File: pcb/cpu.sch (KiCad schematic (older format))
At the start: 76 parts, among them J1 Conn_02x16_Counter_Clockwise, J2 Conn_01x16, U1 74LS283, U2 74LS283, U3 74LS283, U4 74LS283

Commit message: alu function
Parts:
- removed U? (x4): mux16, symbol nand2tetris:mux16
- removed U? (x16): 74AHCT1G04, symbol 74xGxx:74AHCT1G04
- added U? (x3): SN74CBT16233, symbol nand2tetris:SN74CBT16233
- added U? (x32): 74AHCT1G04, symbol 74xGxx:74AHCT1G04
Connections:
- net a0 is gone; now on net x0: J1.1 (Pin_1)
- net a1 is gone; now on net x1: J1.2 (Pin_2)
- net a10 is gone; now on net x10: J1.11 (Pin_11)
- net a11 is gone; now on net x11: J1.12 (Pin_12)
- net a12 is gone; now on net x12: J1.13 (Pin_13)
- net a13 is gone; now on net x13: J1.14 (Pin_14)
- net a14 is gone; now on net x14: J1.15 (Pin_15)
- net a15 is gone; now on net x15: J1.16 (Pin_16)
- net a2 is gone; now on net x2: J1.3 (Pin_3)
- net a3 is gone; now on net x3: J1.4 (Pin_4)
- net a4 is gone; now on net x4: J1.5 (Pin_5)
- net a5 is gone; now on net x5: J1.6 (Pin_6)
- net a6 is gone; now on net x6: J1.7 (Pin_7)
- net a7 is gone; now on net x7: J1.8 (Pin_8)
- net a8 is gone; now on net x8: J1.9 (Pin_9)
- net a9 is gone; now on net x9: J1.10 (Pin_10)
- net b0 is gone; now on net y0: J1.32 (Pin_32)
- net b1 is gone; now on net y1: J1.31 (Pin_31)
- net b10 is gone; now on net y10: J1.22 (Pin_22)
- net b11 is gone; now on net y11: J1.21 (Pin_21)
- net b12 is gone; now on net y12: J1.20 (Pin_20)
- net b13 is gone; now on net y13: J1.19 (Pin_19)
- net b14 is gone; now on net y14: J1.18 (Pin_18)
- net b15 is gone; now on net y15: J1.17 (Pin_17)
- net b2 is gone; now on net y2: J1.30 (Pin_30)
- net b3 is gone; now on net y3: J1.29 (Pin_29)
- net b4 is gone; now on net y4: J1.28 (Pin_28)
- net b5 is gone; now on net y5: J1.27 (Pin_27)
- net b6 is gone; now on net y6: J1.26 (Pin_26)
- net b7 is gone; now on net y7: J1.25 (Pin_25)
- net b8 is gone; now on net y8: J1.24 (Pin_24)
- net b9 is gone; now on net y9: J1.23 (Pin_23)
- net noty0 is gone; now on an unnamed net: U?.4
- net noty1 is gone; now on an unnamed net: U?.4
- net noty10 is gone; now on an unnamed net: U?.4
- net noty11 is gone; now on an unnamed net: U?.4
- net noty12 is gone; now on an unnamed net: U?.4
- net noty13 is gone; now on an unnamed net: U?.4
- net noty14 is gone; now on an unnamed net: U?.4
- net noty15 is gone; now on an unnamed net: U?.4
- net noty2 is gone; now on an unnamed net: U?.4
- net noty3 is gone; now on an unnamed net: U?.4
- net noty4 is gone; now on an unnamed net: U?.4
- net noty5 is gone; now on an unnamed net: U?.4
- net noty6 is gone; now on an unnamed net: U?.4
- net noty7 is gone; now on an unnamed net: U?.4
- net noty8 is gone; now on an unnamed net: U?.4
- net noty9 is gone; now on an unnamed net: U?.4
- net GND: now also U?.44 (GND), U?.3 (GND), U?.3 (GND), U?.3 (GND), U?.3 (GND), U?.3 (GND), U?.3 (GND), U?.3 (GND), U?.3 (GND), U?.3 (GND), U?.3 (GND), U?.3 (GND), U?.3 (GND), U?.3 (GND), U?.3 (GND), U?.3 (GND), U?.3 (GND), U?.3 (GND), U?.3 (GND), U?.3 (GND), U?.3 (GND), U?.3 (GND), U?.3 (GND), U?.3 (GND), U?.3 (GND), U?.3 (GND), U?.3 (GND), U?.3 (GND), U?.3 (GND), U?.3 (GND), U?.3 (GND), U?.3 (GND), U?.3 (GND), U?.44 (GND), U?.44 (GND), U?.44 (GND)
- net VCC: now also U?.43 (VCC), U?.43 (VCC), U?.43 (VCC), U?.43 (VCC), U?.5 (VCC), U?.5 (VCC), U?.5 (VCC), U?.5 (VCC), U?.5 (VCC), U?.5 (VCC), U?.5 (VCC), U?.5 (VCC), U?.5 (VCC), U?.5 (VCC), U?.5 (VCC), U?.5 (VCC), U?.5 (VCC), U?.5 (VCC), U?.5 (VCC), U?.5 (VCC), U?.5 (VCC), U?.5 (VCC), U?.5 (VCC), U?.5 (VCC), U?.5 (VCC), U?.5 (VCC), U?.5 (VCC), U?.5 (VCC), U?.5 (VCC), U?.5 (VCC), U?.5 (VCC), U?.5 (VCC), U?.5 (VCC), U?.5 (VCC), U?.5 (VCC), U?.5 (VCC)
- net band0: now also U?.2
- net band1: now also U?.2
- net band10: now also U?.2
- net band11: now also U?.2
- net band12: now also U?.2
- net band13: now also U?.2
- net band14: now also U?.2
- net band15: now also U?.2
- net band2: now also U?.2
- net band3: now also U?.2
- net band4: now also U?.2
- net band5: now also U?.2
- net band6: now also U?.2
- net band7: now also U?.2
- net band8: no longer U?.3
- net band9: now also U?.2
- net nx: now also U?.30 (SEL1)
- net ny: now also U?.30 (SEL1)
- net opx0: now also U?.1 (1A)
- net opx1: now also U?.54 (2A)
- net opx10: now also U?.18 (11A)
- net opx11: now also U?.37 (12A)
- net opx12: now also U?.21 (13A)
- net opx13: now also U?.34 (14A)
- net opx14: now also U?.24 (15A)
- net opx15: now also U?.31 (16A)
- net opx2: now also U?.4 (3A)
- net opx3: now also U?.51 (4A)
- net opx4: now also U?.7 (5A)
- net opx5: now also U?.48 (6A)
- net opx6: now also U?.10 (7A)
- net opx7: now also U?.45 (8A)
- net opx8: now also U?.15 (9A)
- net opx9: now also U?.40 (10A)
- net zdx0: now also U?.1 (1A), U?.2, U?.56 (1B1)
- net zdx1: now also U?.2, U?.2 (2B1), U?.54 (2A)
- net zdx10: now also U?.18 (11A), U?.2, U?.39 (11B1)
- net zdx11: now also U?.19 (12B1), U?.2, U?.37 (12A)
- net zdx12: now also U?.2, U?.21 (13A), U?.36 (13B1)
- net zdx13: now also U?.2, U?.22 (14B1), U?.34 (14A)
- net zdx14: now also U?.2, U?.24 (15A), U?.33 (15B1)
- net zdx15: now also U?.2, U?.25 (16B1), U?.31 (16A)
- net zdx2: now also U?.2, U?.4 (3A), U?.53 (3B1)
- net zdx3: now also U?.2, U?.5 (4B1), U?.51 (4A)
- net zdx4: now also U?.2, U?.50 (5B1), U?.7 (5A)
- net zdx5: now also U?.2, U?.48 (6A), U?.8 (6B1)
- net zdx6: now also U?.10 (7A), U?.2, U?.47 (7B1)
- net zdx7: now also U?.11 (8B1), U?.2, U?.45 (8A)
- net zdx8: now also U?.15 (9A), U?.2, U?.42 (9B1)
- net zdx9: now also U?.16 (10B1), U?.2, U?.40 (10A)
- net zdy0: now also U?.56 (1B1), U?.1 (1A)
- net zdy1: now also U?.2 (2B1), U?.54 (2A)
- net zdy10: now also U?.39 (11B1), U?.18 (11A)
- net zdy11: now also U?.19 (12B1), U?.37 (12A)
- net zdy12: now also U?.36 (13B1), U?.21 (13A)
- net zdy13: now also U?.22 (14B1), U?.34 (14A)
- net zdy14: now also U?.33 (15B1), U?.24 (15A)
- net zdy15: now also U?.25 (16B1), U?.31 (16A)
- net zdy2: now also U?.53 (3B1), U?.4 (3A)
- net zdy3: now also U?.5 (4B1), U?.51 (4A)
- net zdy4: now also U?.50 (5B1), U?.7 (5A)
- net zdy5: now also U?.8 (6B1), U?.48 (6A)
- net zdy6: now also U?.47 (7B1), U?.10 (7A)
- net zdy7: now also U?.11 (8B1), U?.45 (8A)
- net zdy8: now also U?.42 (9B1), U?.15 (9A)
- net zdy9: now also U?.16 (10B1), U?.40 (10A)
- net zx: now also U?.30 (SEL1)
- net zy: now also U?.30 (SEL1)
- new net: U?.2, U?.3
- new net: U?.12 (8B2), U?.4
- new net: U?.4, U?.46 (7B2)
- new net: U?.4, U?.9 (6B2)
- new net: U?.4, U?.49 (5B2)
- new net: U?.4, U?.6 (4B2)
- new net: U?.4, U?.52 (3B2)
- new net: U?.3 (2B2), U?.4
- new net: U?.4, U?.55 (1B2)
- new net: U?.26 (16B2), U?.4
- new net: U?.32 (15B2), U?.4
- new net: U?.23 (14B2), U?.4
- new net: U?.35 (13B2), U?.4
- new net: U?.20 (12B2), U?.4
- new net: U?.38 (11B2), U?.4
- new net: U?.17 (10B2), U?.4
- new net: U?.4, U?.41 (9B2)
- new net notband0: U?.4
- new net notband1: U?.4
- new net notband10: U?.4
- new net notband11: U?.4
- new net notband12: U?.4
- new net notband13: U?.4
- new net notband14: U?.4
- new net notband15: U?.4
- new net notband2: U?.4
- new net notband3: U?.4
- new net notband4: U?.4
- new net notband5: U?.4
- new net notband6: U?.4
- new net notband7: U?.4
- new net notband8: U?.4
- new net notband9: U?.4
- no-connect marks 2 -> 22
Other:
- moved on the sheet: J1, J2, J?, U1, U2, U3, U4, U?, U?A

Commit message: output select
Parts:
- added U? (x3): SN74CBT16233, symbol nand2tetris:SN74CBT16233
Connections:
- net GND: now also U?.44 (GND), U?.44 (GND), U?.44 (GND)
- net VCC: now also U?.43 (VCC), U?.43 (VCC), U?.43 (VCC)
- net band0: now also U?.56 (1B1)
- net band1: now also U?.2 (2B1)
- net band10: now also U?.39 (11B1)
- net band11: now also U?.19 (12B1)
- net band12: now also U?.36 (13B1)
- net band13: now also U?.22 (14B1)
- net band14: now also U?.33 (15B1)
- net band15: now also U?.25 (16B1)
- net band2: now also U?.53 (3B1)
- net band3: now also U?.5 (4B1)
- net band4: now also U?.50 (5B1)
- net band5: now also U?.8 (6B1)
- net band6: now also U?.47 (7B1)
- net band7: now also U?.11 (8B1)
- net band8: now also U?.42 (9B1)
- net band9: now also U?.16 (10B1)
- net f: now also U?.30 (SEL1), U?.30 (SEL1)
- net no: now also U?.30 (SEL1)
- net notband0: now also U?.56 (1B1)
- net notband1: now also U?.2 (2B1)
- net notband10: now also U?.39 (11B1)
- net notband11: now also U?.19 (12B1)
- net notband12: now also U?.36 (13B1)
- net notband13: now also U?.22 (14B1)
- net notband14: now also U?.33 (15B1)
- net notband15: now also U?.25 (16B1)
- net notband2: now also U?.53 (3B1)
- net notband3: now also U?.5 (4B1)
- net notband4: now also U?.50 (5B1)
- net notband5: now also U?.8 (6B1)
- net notband6: now also U?.47 (7B1)
- net notband7: now also U?.11 (8B1)
- net notband8: now also U?.42 (9B1)
- net notband9: now also U?.16 (10B1)
- net sum0: now also U?.55 (1B2)
- net sum1: now also U?.3 (2B2)
- net sum10: now also U?.38 (11B2)
- net sum11: now also U?.20 (12B2)
- net sum12: now also U?.35 (13B2)
- net sum13: now also U?.23 (14B2)
- net sum14: now also U?.32 (15B2)
- net sum15: now also U?.26 (16B2)
- net sum2: now also U?.52 (3B2)
- net sum3: now also U?.6 (4B2)
- net sum4: now also U?.49 (5B2)
- net sum5: now also U?.9 (6B2)
- net sum6: now also U?.46 (7B2)
- net sum7: now also U?.12 (8B2)
- net sum8: now also U?.41 (9B2)
- net sum9: now also U?.17 (10B2)
- new net: U?.1 (1A), U?.56 (1B1)
- new net: U?.10 (7A), U?.47 (7B1)
- new net: U?.15 (9A), U?.42 (9B1)
- new net: U?.18 (11A), U?.39 (11B1)
- new net: U?.21 (13A), U?.36 (13B1)
- new net: U?.24 (15A), U?.33 (15B1)
- new net: U?.25 (16B1), U?.31 (16A)
- new net: U?.22 (14B1), U?.34 (14A)
- new net: U?.19 (12B1), U?.37 (12A)
- new net: U?.4 (3A), U?.53 (3B1)
- new net: U?.16 (10B1), U?.40 (10A)
- new net: U?.11 (8B1), U?.45 (8A)
- new net: U?.48 (6A), U?.8 (6B1)
- new net: U?.5 (4B1), U?.51 (4A)
- new net: U?.2 (2B1), U?.54 (2A)
- new net: U?.50 (5B1), U?.7 (5A)
- new net notsum: U?.12 (8B2), U?.17 (10B2), U?.20 (12B2), U?.23 (14B2), U?.26 (16B2), U?.3 (2B2), U?.32 (15B2), U?.35 (13B2), U?.38 (11B2), U?.41 (9B2), U?.46 (7B2), U?.49 (5B2), U?.52 (3B2), U?.55 (1B2), U?.6 (4B2), U?.9 (6B2)
- new net oalu0: U?.1 (1A)
- new net oalu1: U?.54 (2A)
- new net oalu10: U?.18 (11A)
- new net oalu11: U?.37 (12A)
- new net oalu12: U?.21 (13A)
- new net oalu13: U?.34 (14A)
- new net oalu14: U?.24 (15A)
- new net oalu15: U?.31 (16A)
- new net oalu2: U?.4 (3A)
- new net oalu3: U?.51 (4A)
- new net oalu4: U?.7 (5A)
- new net oalu5: U?.48 (6A)
- new net oalu6: U?.10 (7A)
- new net oalu7: U?.45 (8A)
- new net oalu8: U?.15 (9A)
- new net oalu9: U?.40 (10A)
- new net selnot0: U?.1 (1A), U?.55 (1B2)
- new net selnot1: U?.3 (2B2), U?.54 (2A)
- new net selnot10: U?.18 (11A), U?.38 (11B2)
- new net selnot11: U?.20 (12B2), U?.37 (12A)
- new net selnot12: U?.21 (13A), U?.35 (13B2)
- new net selnot13: U?.23 (14B2), U?.34 (14A)
- new net selnot14: U?.24 (15A), U?.32 (15B2)
- new net selnot15: U?.26 (16B2), U?.31 (16A)
- new net selnot2: U?.4 (3A), U?.52 (3B2)
- new net selnot3: U?.51 (4A), U?.6 (4B2)
- new net selnot4: U?.49 (5B2), U?.7 (5A)
- new net selnot5: U?.48 (6A), U?.9 (6B2)
- new net selnot6: U?.10 (7A), U?.46 (7B2)
- new net selnot7: U?.12 (8B2), U?.45 (8A)
- new net selnot8: U?.15 (9A), U?.41 (9B2)
- new net selnot9: U?.17 (10B2), U?.40 (10A)
- no-connect marks 22 -> 37

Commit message: ALU
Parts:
- added U? (x15): 74LS32, symbol 74xx:74LS32
- added U? (x15): 74LS02, symbol 74xx:74LS02
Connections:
- net oalu0: now also U?.2
- net oalu1: now also U?.3
- net oalu10: now also U?.2
- net oalu11: now also U?.3
- net oalu12: now also U?.2
- net oalu13: now also U?.3
- net oalu14: now also U?.2
- net oalu2: now also U?.2
- net oalu3: now also U?.3
- net oalu4: now also U?.2
- net oalu5: now also U?.3
- net oalu6: now also U?.2
- net oalu7: now also U?.3
- net oalu8: now also U?.2
- net oalu9: now also U?.3
- net oalu15 renamed ng
- net ng: now also U?.3
- new net: U?.1, U?.3 (x14)
- new net: U?.2, U?.3 (x7)
- new net: U?.1, U?.2 (x7)
- new net zr: U?.1

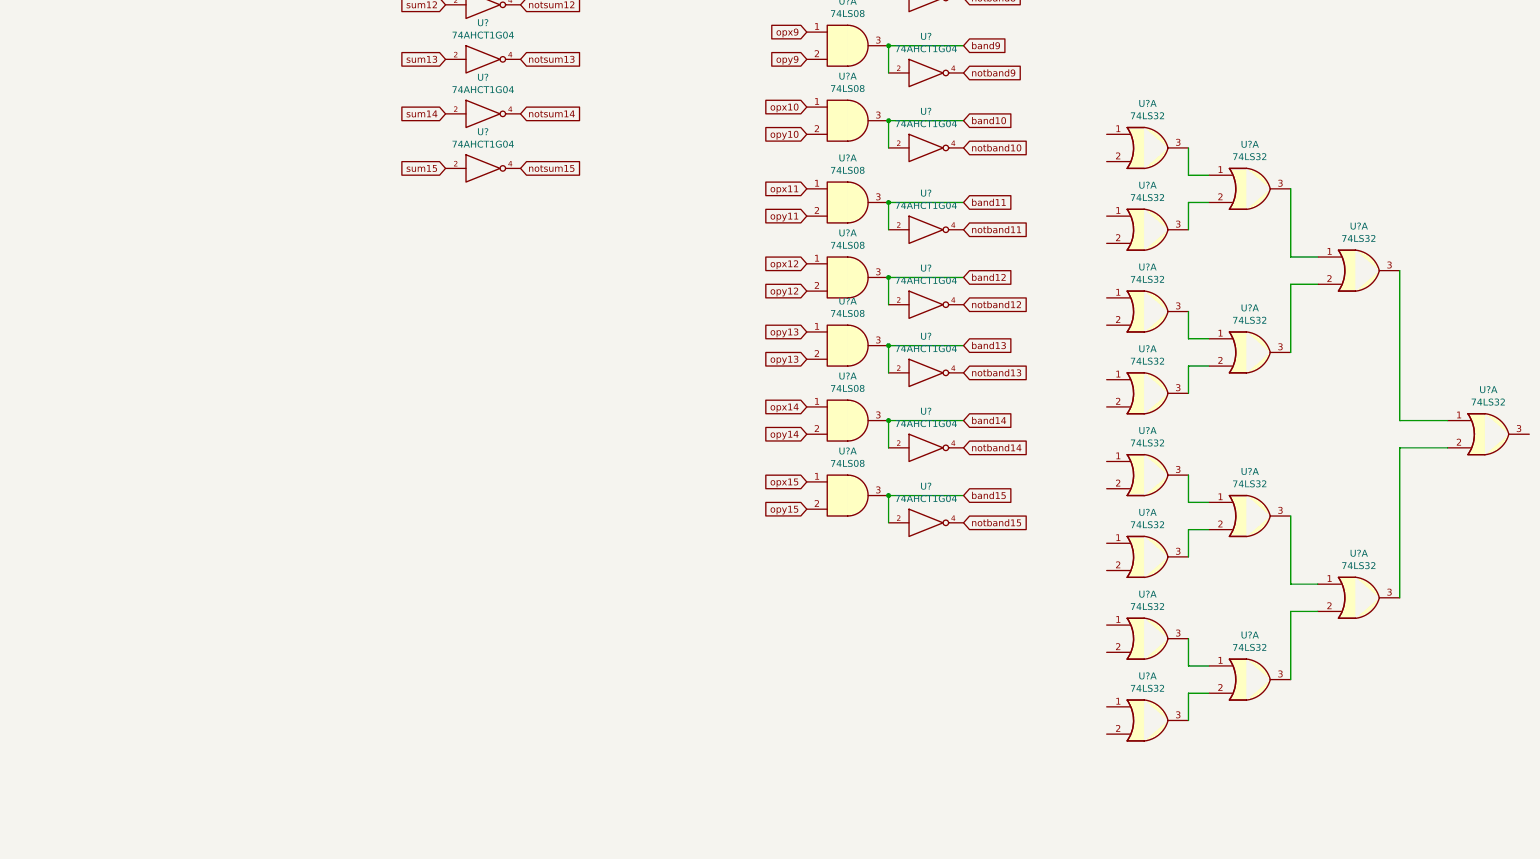
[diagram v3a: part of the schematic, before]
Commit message: RAM symbol
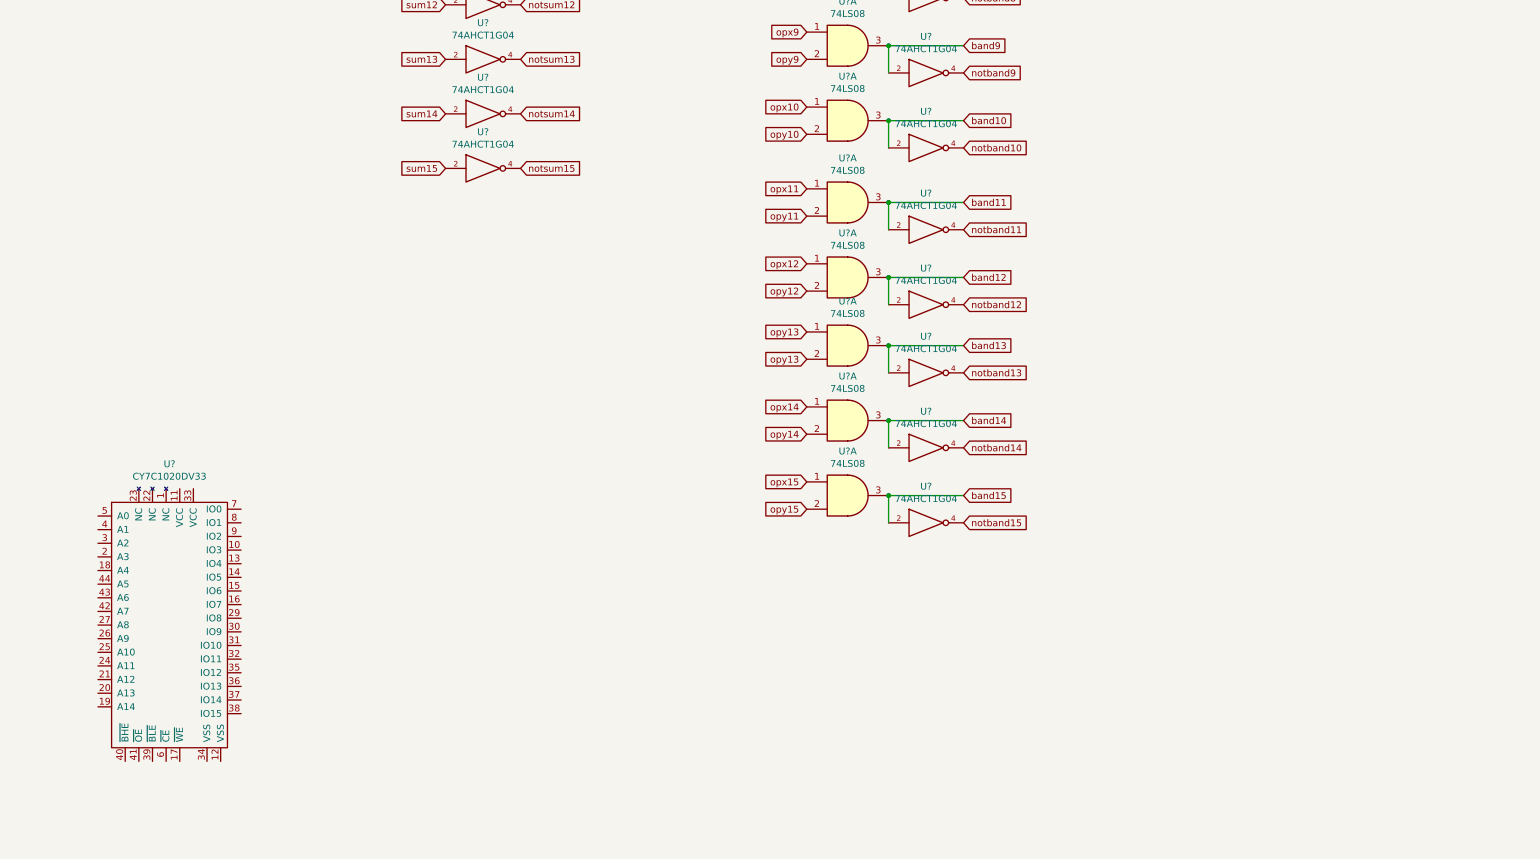
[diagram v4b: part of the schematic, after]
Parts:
- removed U? (x15): 74LS32, symbol 74xx:74LS32
- added U?: CY7C1020DV33, symbol nand2tetris:CY7C1020DV33
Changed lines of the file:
@@
 Text GLabel 7050 8750 2    50   Input ~ 0
 oalu15
-$Comp
-L 74xx:74LS32 U?
-U 1 1 5EC51D7B
-P 20800 9700
-F 0 "U?" H 20800 10025 50  0000 C CNN
-F 1 "74LS32" H 20800 9934 50  0000 C CNN
-F 2 "" H 20800 9700 50  0001 C CNN
-F 3 "http://www.ti.com/lit/gpn/sn74LS32" H 20800 9700 50  0001 C CNN
-	1    20800 9700
-	1    0    0    -1
-$EndComp
-$Comp
-L 74xx:74LS32 U?
-U 1 1 5EC5C63C
-P 22550 11500
-F 0 "U?" H 22550 11825 50  0000 C CNN
-F 1 "74LS32" H 22550 11734 50  0000 C CNN
-F 2 "" H 22550 11500 50  0001 C CNN
-F 3 "http://www.ti.com/lit/gpn/sn74LS32" H 22550 11500 50  0001 C CNN
-	1    22550 11500
-	1    0    0    -1
-$EndComp
-Wire Wire Line
-	20350 9600 20500 9600
-Wire Wire Line
-	20350 10000 20350 9800
-Wire Wire Line
-	20350 9800 20500 9800
-Wire Wire Line
-	20350 9400 20350 9600
-$Comp
-L 74xx:74LS32 U?
-U 1 1 5EDC87A5
-P 20050 10600
-F 0 "U?" H 20050 10925 50  0000 C CNN
-F 1 "74LS32" H 20050 10834 50  0000 C CNN
-F 2 "" H 20050 10600 50  0001 C CNN
-F 3 "http://www.ti.com/lit/gpn/sn74LS32" H 20050 10600 50  0001 C CNN
-	1    20050 10600
-	1    0    0    -1
-$EndComp
-$Comp
-L 74xx:74LS32 U?
-U 1 1 5EDC87AB
-P 20050 11200
-F 0 "U?" H 20050 11525 50  0000 C CNN
-F 1 "74LS32" H 20050 11434 50  0000 C CNN
-F 2 "" H 20050 11200 50  0001 C CNN
-F 3 "http://www.ti.com/lit/gpn/sn74LS32" H 20050 11200 50  0001 C CNN
-	1    20050 11200
-	1    0    0    -1
-$EndComp
-Wire Wire Line
-	20350 10800 20500 10800
-Wire Wire Line
-	20350 11200 20350 11000
-Wire Wire Line
-	20350 11000 20500 11000
-Wire Wire Line
-	20350 10600 20350 10800
-$Comp
-L 74xx:74LS32 U?
-U 1 1 5EDECCE9
-P 20050 11800
-F 0 "U?" H 20050 12125 50  0000 C CNN
-F 1 "74LS32" H 20050 12034 50  0000 C CNN
-F 2 "" H 20050 11800 50  0001 C CNN
-F 3 "http://www.ti.com/lit/gpn/sn74LS32" H 20050 11800 50  0001 C CNN
-	1    20050 11800
-	1    0    0    -1
-$EndComp
-$Comp
-L 74xx:74LS32 U?
-U 1 1 5EDECCEF
-P 20050 12400
-F 0 "U?" H 20050 12725 50  0000 C CNN
-F 1 "74LS32" H 20050 12634 50  0000 C CNN
-F 2 "" H 20050 12400 50  0001 C CNN
-F 3 "http://www.ti.com/lit/gpn/sn74LS32" H 20050 12400 50  0001 C CNN
-	1    20050 12400
-	1    0    0    -1
-$EndComp
-$Comp
-L 74xx:74LS32 U?
-U 1 1 5EDECCF5
-P 20800 12100
-F 0 "U?" H 20800 12425 50  0000 C CNN
-F 1 "74LS32" H 20800 12334 50  0000 C CNN
-F 2 "" H 20800 12100 50  0001 C CNN
-F 3 "http://www.ti.com/lit/gpn/sn74LS32" H 20800 12100 50  0001 C CNN
-	1    20800 12100
-	1    0    0    -1
-$EndComp
-Wire Wire Line
-	20350 12000 20500 12000
-Wire Wire Line
-	20350 12400 20350 12200
-Wire Wire Line
-	20350 12200 20500 12200
-Wire Wire Line
-	20350 11800 20350 12000
-$Comp
-L 74xx:74LS32 U?
-U 1 1 5EDC87B1
-P 20800 10900
-F 0 "U?" H 20800 11225 50  0000 C CNN
-F 1 "74LS32" H 20800 11134 50  0000 C CNN
-F 2 "" H 20800 10900 50  0001 C CNN
-F 3 "http://www.ti.com/lit/gpn/sn74LS32" H 20800 10900 50  0001 C CNN
-	1    20800 10900
-	1    0    0    -1
-$EndComp
-$Comp
-L 74xx:74LS32 U?
-U 1 1 5EC58931
-P 21600 10300
-F 0 "U?" H 21600 10625 50  0000 C CNN
-F 1 "74LS32" H 21600 10534 50  0000 C CNN
-F 2 "" H 21600 10300 50  0001 C CNN
-F 3 "http://www.ti.com/lit/gpn/sn74LS32" H 21600 10300 50  0001 C CNN
-	1    21600 10300
-	1    0    0    -1
-$EndComp
-$Comp
-L 74xx:74LS32 U?
-U 1 1 5EECAE86
-P 20050 13000
-F 0 "U?" H 20050 13325 50  0000 C CNN
-F 1 "74LS32" H 20050 13234 50  0000 C CNN
-F 2 "" H 20050 13000 50  0001 C CNN
-F 3 "http://www.ti.com/lit/gpn/sn74LS32" H 20050 13000 50  0001 C CNN
-	1    20050 13000
-	1    0    0    -1
-$EndComp
-$Comp
-L 74xx:74LS32 U?
-U 1 1 5EECAE8C
-P 20050 13600
-F 0 "U?" H 20050 13925 50  0000 C CNN
-F 1 "74LS32" H 20050 13834 50  0000 C CNN
-F 2 "" H 20050 13600 50  0001 C CNN
-F 3 "http://www.ti.com/lit/gpn/sn74LS32" H 20050 13600 50  0001 C CNN
-	1    20050 13600
-	1    0    0    -1
-$EndComp
-$Comp
-L 74xx:74LS32 U?
-U 1 1 5EECAE92
-P 20800 13300
-F 0 "U?" H 20800 13625 50  0000 C CNN
-F 1 "74LS32" H 20800 13534 50  0000 C CNN
-F 2 "" H 20800 13300 50  0001 C CNN
-F 3 "http://www.ti.com/lit/gpn/sn74LS32" H 20800 13300 50  0001 C CNN
-	1    20800 13300
-	1    0    0    -1
-$EndComp
-Wire Wire Line
-	20350 13200 20500 13200
-Wire Wire Line
-	20350 13600 20350 13400
-Wire Wire Line
-	20350 13400 20500 13400
-Wire Wire Line
-	20350 13000 20350 13200
-Wire Wire Line
-	21100 9700 21100 10200
-Wire Wire Line
-	21100 10200 21300 10200
-Wire Wire Line
-	21100 10400 21300 10400
-Wire Wire Line
-	21100 10400 21100 10900
-$Comp
-L 74xx:74LS32 U?
-U 1 1 5EF6167A
-P 21600 12700
-F 0 "U?" H 21600 13025 50  0000 C CNN
-F 1 "74LS32" H 21600 12934 50  0000 C CNN
-F 2 "" H 21600 12700 50  0001 C CNN
-F 3 "http://www.ti.com/lit/gpn/sn74LS32" H 21600 12700 50  0001 C CNN
-	1    21600 12700
-	1    0    0    -1
-$EndComp
-Wire Wire Line
-	21100 12100 21100 12600
-Wire Wire Line
-	21100 12600 21300 12600
-Wire Wire Line
-	21100 12800 21300 12800
-Wire Wire Line
-	21100 12800 21100 13300
-Wire Wire Line
-	21900 10300 21900 11400
-Wire Wire Line
-	21900 11400 22250 11400
-Wire Wire Line
-	21900 12700 21900 11600
-Wire Wire Line
-	21900 11600 22250 11600
-$Comp
-L 74xx:74LS32 U?
-U 1 1 5EC4A9FA
-P 20050 10000
-F 0 "U?" H 20050 10325 50  0000 C CNN
-F 1 "74LS32" H 20050 10234 50  0000 C CNN
-F 2 "" H 20050 10000 50  0001 C CNN
-F 3 "http://www.ti.com/lit/gpn/sn74LS32" H 20050 10000 50  0001 C CNN
-	1    20050 10000
-	1    0    0    -1
-$EndComp
-$Comp
-L 74xx:74LS32 U?
-U 1 1 5EC45C12
-P 20050 9400
-F 0 "U?" H 20050 9725 50  0000 C CNN
-F 1 "74LS32" H 20050 9634 50  0000 C CNN
-F 2 "" H 20050 9400 50  0001 C CNN
-F 3 "http://www.ti.com/lit/gpn/sn74LS32" H 20050 9400 50  0001 C CNN
-	1    20050 9400
-	1    0    0    -1
-$EndComp
 Wire Wire Line
 	8800 7650 8950 7650
@@
 Wire Wire Line
 	7050 8850 6900 8850
+$Comp
+L nand2tetris:CY7C1020DV33 U?
+U 1 1 5F60485E
+P 12900 12850
+F 0 "U?" H 12875 13981 50  0000 C CNN
+F 1 "CY7C1020DV33" H 12875 13890 50  0000 C CNN
+F 2 "" H 12900 11200 50  0001 C CNN
+F 3 "https://cz.mouser.com/datasheet/2/100/CY7C1020DV33_38-05461_0I_V-258968.pdf" H 12900 11200 50  0001 C CNN
+	1    12900 12850
+	1    0    0    -1
+$EndComp
 Wire Bus Line
 	7850 7100 7850 11650

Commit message: WIP memory
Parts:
- added U? (x2): 74AUC1G18, symbol 74xGxx:74AUC1G18
- added U?: 74AHCT1G04, symbol 74xGxx:74AHCT1G04
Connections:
- net GND: now also U?.2 (GND), U?.2 (GND), U?.3 (GND)
- net VCC: now also U?.5 (VCC), U?.5 (VCC), U?.5 (VCC)
- net at U?.17 (~WE~): now also U?.4
- net low: now reaches U?.39 (~BLE~)
- net low: now also U?.40 (~BHE~)
- new net adr13: U?.1
- new net adr14: U?.1
- new net lkbd: U?.4
- new net load: U?.3
- new net lram: U?.2, U?.6
- new net lvram: U?.6
- new net nlram: U?.3, U?.4
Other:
- note added: "read/write 16 bits"
- moved on the sheet: U?, U?A
